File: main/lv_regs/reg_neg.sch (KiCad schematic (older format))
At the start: 10 parts, among them M2 ﻿APXW003A0X3-SRZ

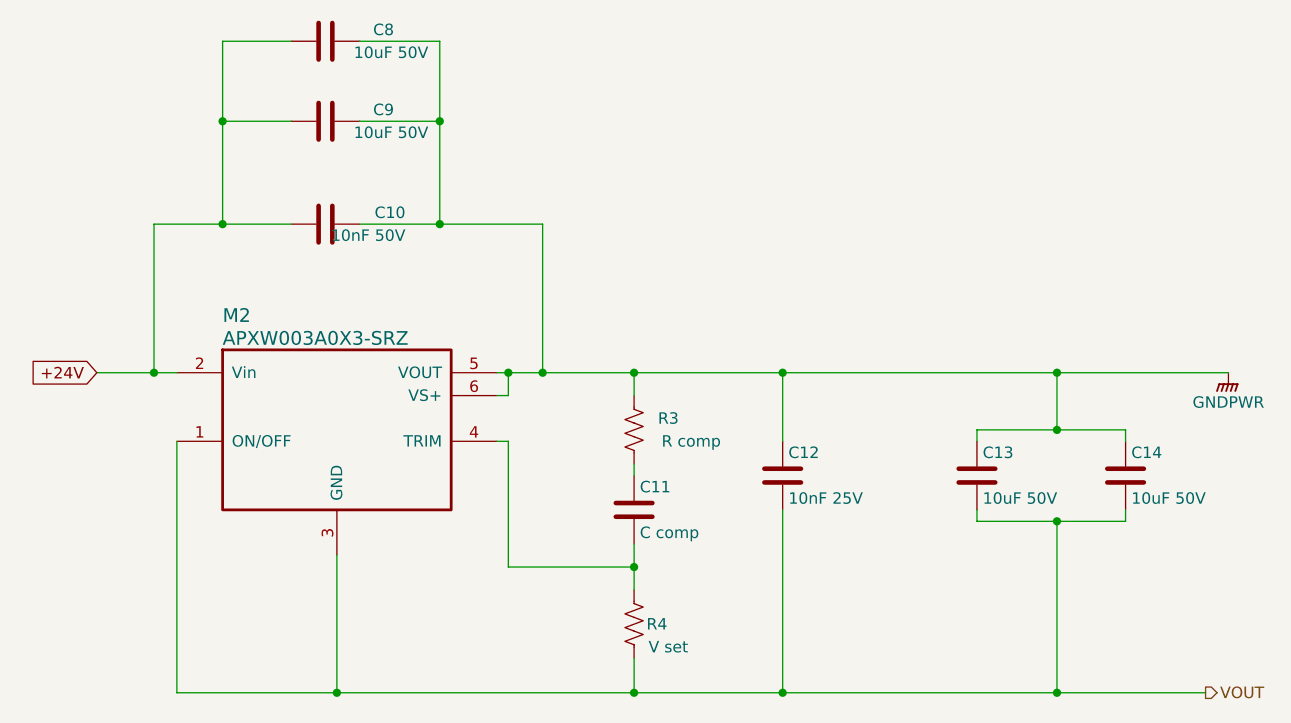
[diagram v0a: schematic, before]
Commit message: A near final version of the low-volt regulator board. Pending footprint comparison on the actual parts.
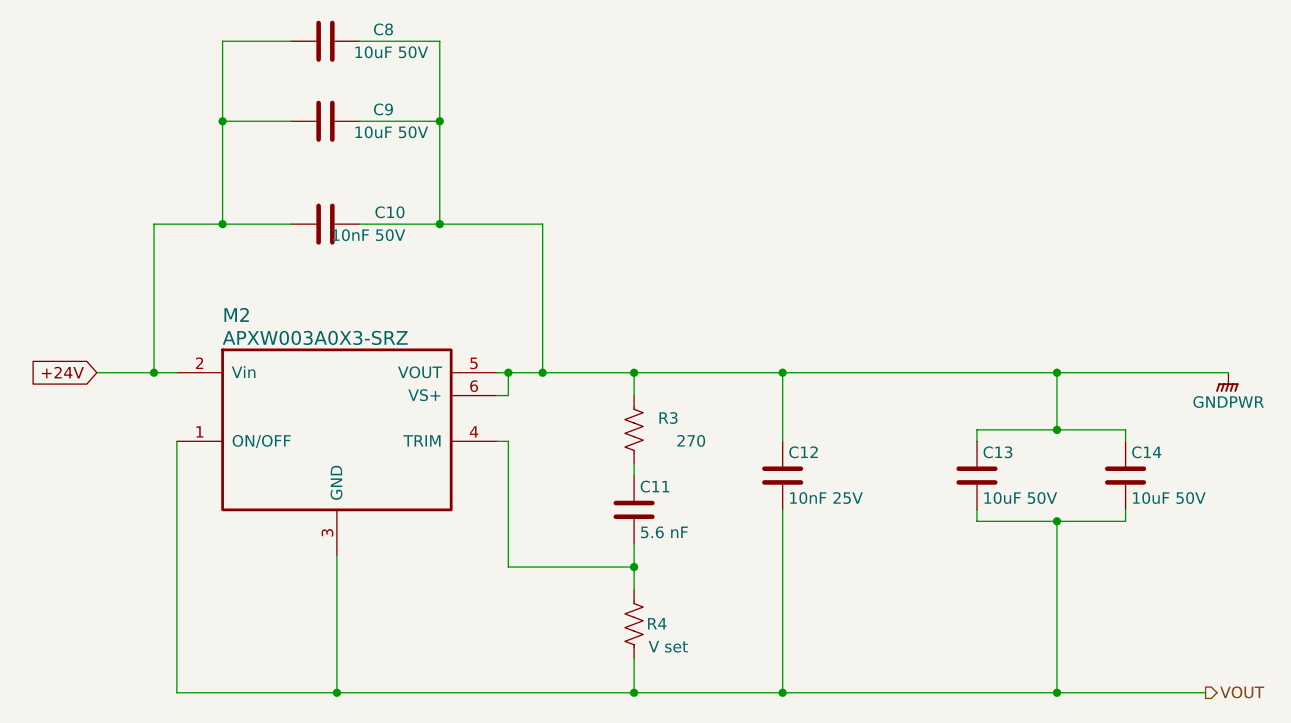
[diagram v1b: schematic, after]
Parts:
- C10: DK line (none) -> P.5
- C11: value C comp -> 5.6 nF
- C12: DK line (none) -> P.2
- C13, C14, C8, C9: DK line (none) -> P.4
- M2: DK line (none) -> P.1
- R3: value R comp -> 270
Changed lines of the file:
@@
 F 6 "APXW003A0X3-SRZ" H 4900 2900 50  0001 C CNN "MPN"
 F 7 "ABB Power Electronics Inc." H 4900 2900 50  0001 C CNN "Manufacturer"
+F 8 "P.1" H 4900 2900 50  0001 C CNN "DK line"
 	1    4900 2900
 	1    0    0    -1
@@
 F 6 "LLL185R71E103MA01L" H 7550 3350 50  0001 C CNN "MPN"
 F 7 "Murata Electronics" H 7550 3350 50  0001 C CNN "Manufacturer"
+F 8 "P.2" H 7550 3350 50  0001 C CNN "DK line"
 	1    7550 3350
 	1    0    0    -1
@@
 F 6 "C0603C103M5RACTU" H 5550 2250 50  0001 C CNN "MPN"
 F 7 "KEMET" H 5550 2250 50  0001 C CNN "Manufacturer"
+F 8 "P.5" H 5550 2250 50  0001 C CNN "DK line"
 	1    5550 2250
 	0    -1   -1   0
@@
 F 6 "CL32B106KBJNNNE" H 5550 1800 50  0001 C CNN "MPN"
 F 7 "Samsung Electro-Mechanics" H 5550 1800 50  0001 C CNN "Manufacturer"
+F 8 "P.4" H 5550 1800 50  0001 C CNN "DK line"
 	1    5550 1800
 	0    -1   -1   0
@@
 F 6 "CL32B106KBJNNNE" H 5550 1450 50  0001 C CNN "MPN"
 F 7 "Samsung Electro-Mechanics" H 5550 1450 50  0001 C CNN "Manufacturer"
+F 8 "P.4" H 5550 1450 50  0001 C CNN "DK line"
 	1    5550 1450
 	0    -1   -1   0
@@
 AR Path="/5F2135EF/5F217C3C" Ref="R3"  Part="1"
 F 0 "R3" H 7050 3200 50  0000 C CNN
-F 1 "R comp" H 7150 3100 50  0000 C CNN
+F 1 "270" H 7150 3100 50  0000 C CNN
 F 2 "Resistor_SMD:R_0603_1608Metric" V 6940 3140 50  0001 C CNN
 F 3 "~" H 6900 3150 50  0001 C CNN
@@
 AR Path="/5F2135EF/5F217C48" Ref="C11"  Part="1"
 F 0 "C11" H 6925 3600 50  0000 L CNN
-F 1 "C comp" H 6925 3400 50  0000 L CNN
+F 1 "5.6 nF" H 6925 3400 50  0000 L CNN
 F 2 "Capacitor_SMD:C_0603_1608Metric" H 6938 3350 50  0001 C CNN
 F 3 "~" H 6900 3500 50  0001 C CNN
@@
 F 6 "CL32B106KBJNNNE" H 8400 3350 50  0001 C CNN "MPN"
 F 7 "Samsung Electro-Mechanics" H 8400 3350 50  0001 C CNN "Manufacturer"
+F 8 "P.4" H 8400 3350 50  0001 C CNN "DK line"
 	1    8400 3350
 	1    0    0    -1
@@
 F 6 "CL32B106KBJNNNE" H 9050 3350 50  0001 C CNN "MPN"
 F 7 "Samsung Electro-Mechanics" H 9050 3350 50  0001 C CNN "Manufacturer"
+F 8 "P.4" H 9050 3350 50  0001 C CNN "DK line"
 	1    9050 3350
 	1    0    0    -1

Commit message: Schematic revision for DAC board, compensation tweaks in lv_regs.
Opamp +/- pins were swapped in reference_buffer.sch as side effect of the symbol change from using a dual opamp.

lv_regs files.  The compensation components were (CTUNE/RTUNE) were quite wrong, and everything oscillated like crazy. The positive regulators are fine with no compensation, and the negative regulator benefits from a bit.
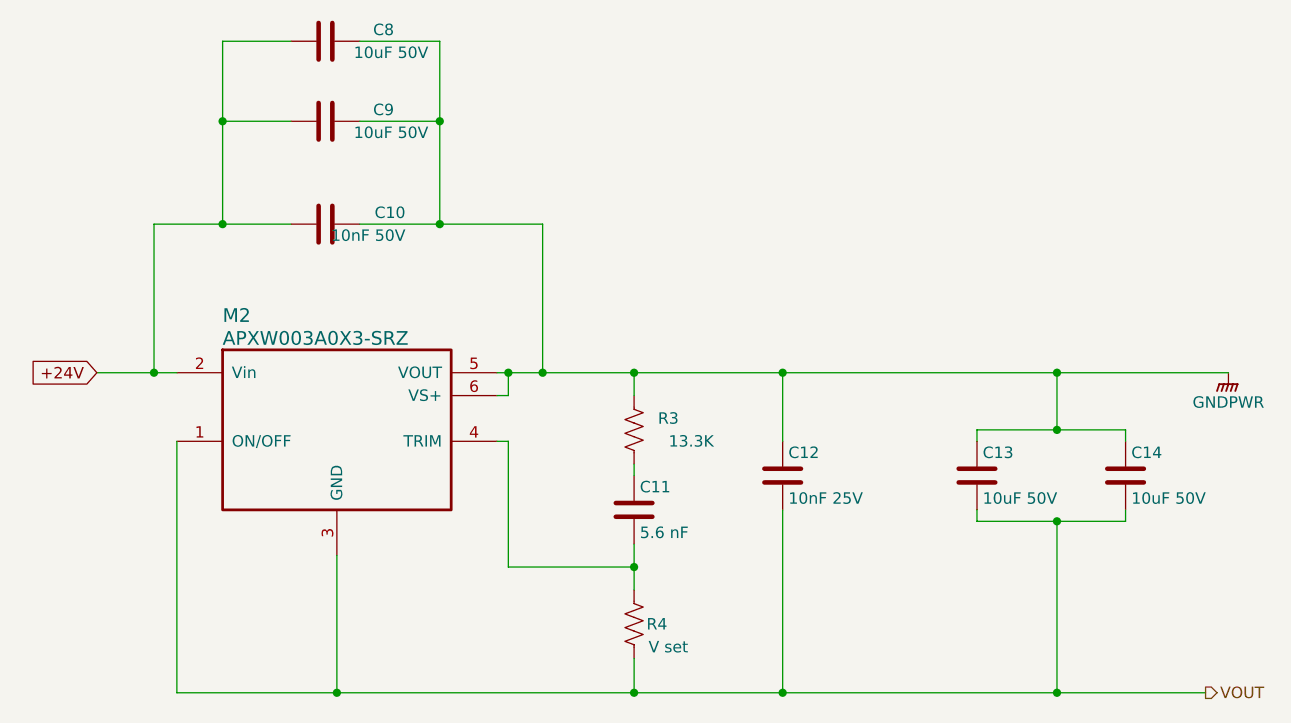
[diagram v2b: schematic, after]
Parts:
- R3: value 270 -> 13.3K
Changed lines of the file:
@@
 AR Path="/5F2135EF/5F217C3C" Ref="R3"  Part="1"
 F 0 "R3" H 7050 3200 50  0000 C CNN
-F 1 "270" H 7150 3100 50  0000 C CNN
+F 1 "13.3K" H 7150 3100 50  0000 C CNN
 F 2 "Resistor_SMD:R_0603_1608Metric" V 6940 3140 50  0001 C CNN
 F 3 "~" H 6900 3150 50  0001 C CNN
